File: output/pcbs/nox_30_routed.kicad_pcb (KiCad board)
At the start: 2 copper layers, 120.3 x 88.1 mm, 70 parts

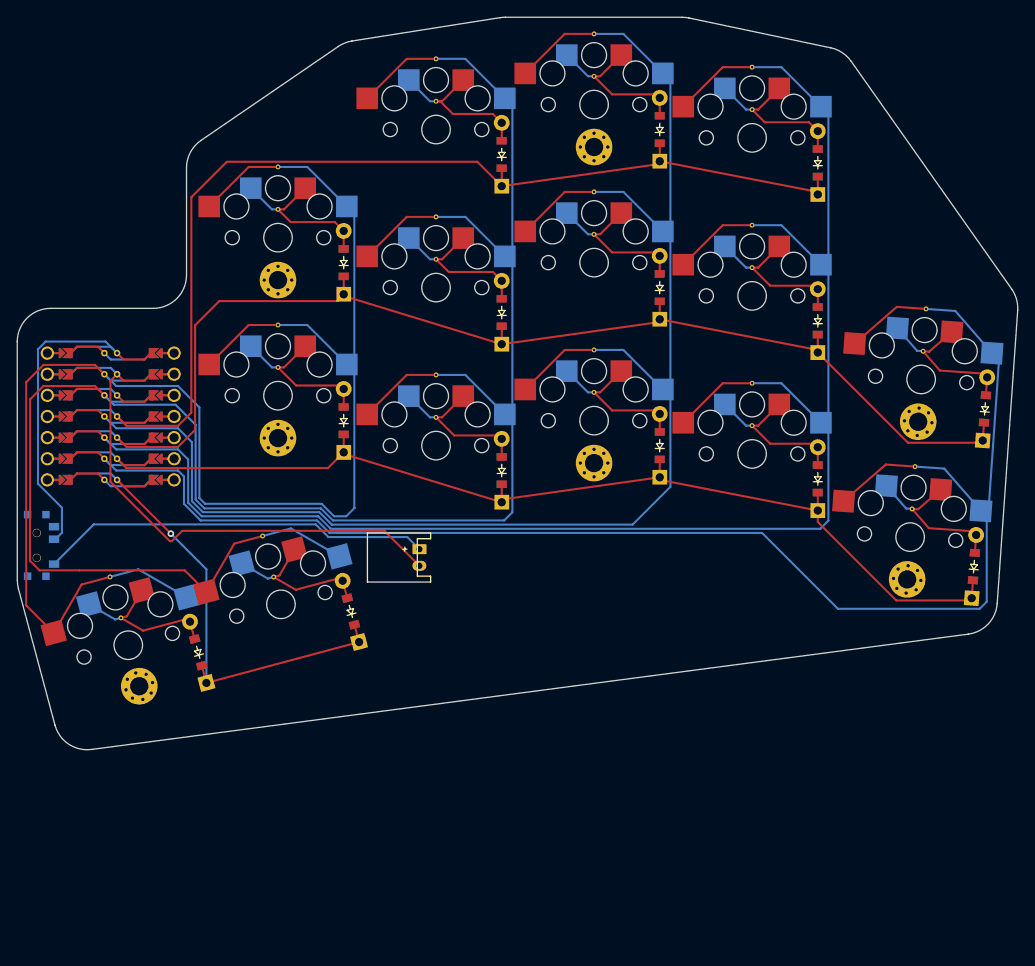
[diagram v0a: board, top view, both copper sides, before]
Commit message: 18 key layout
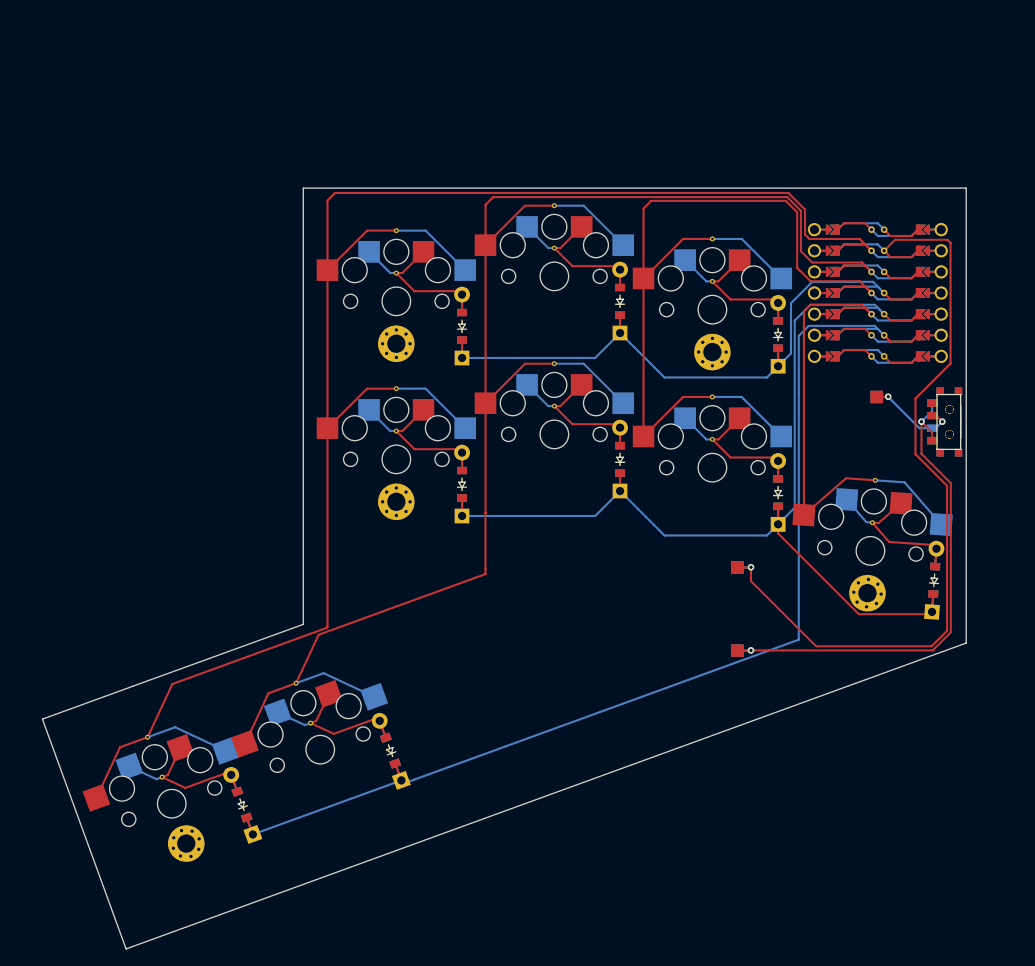
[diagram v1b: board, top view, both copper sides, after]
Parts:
- removed D10, D11, D12, D13, D14, D15: , ComboDiode
- removed JST1: , JST_PH_S2B-PH-K_02x2.00mm_Angled
- removed the REF** at (33.1, 90.2)
- removed the REF** at (50.1, 80.4)
- removed the REF** at (90.0, 58.0)
- removed the REF** at (71.0, 28.1)
- removed the REF** at (71.0, 42.0)
- removed the REF** at (128.5, 72.0)
- removed the REF** at (71.0, 23.0)
- removed the REF** at (52.0, 55.0)
- removed the REF** at (51.4, 85.3)
- removed the REF** at (71.0, 61.0)
- removed the REF** at (128.2, 77.1)
- removed the REF** at (109.0, 62.0)
- removed the REF** at (109.0, 67.1)
- removed the REF** at (109.0, 24.0)
- removed the REF** at (52.0, 60.1)
- removed the REF** at (90.0, 20.0)
- removed the REF** at (129.5, 58.2)
- removed the REF** at (90.0, 25.1)
- removed the REF** at (109.0, 48.1)
- removed the REF** at (109.0, 43.0)
- removed the REF** at (90.0, 44.1)
- removed the REF** at (90.0, 63.1)
- removed the REF** at (71.0, 66.1)
- removed the REF** at (90.0, 39.0)
- removed the REF** at (31.8, 85.3)
- removed the REF** at (52.0, 41.1)
- removed the REF** at (129.9, 53.1)
- removed the REF** at (52.0, 36.0)
- removed the REF** at (71.0, 47.1)
- removed the REF** at (109.0, 29.1)
- removed S10, S11, S12, S13, S14, S15: , PG1350
- removed _31, _32, _33, _34, _35, _36, _37: , MountingHole_2.2mm_M2_Pad_Via
- added BATTPAD1: , ComboDiode, F.Cu at (107.2, 89.2)
- added PAD1: , SMDPad, F.Cu at (123.9, 63.7)
- added REF**: VIA-0.6mm, VIA-0.6mm, F.Cu at (66.2, 62.7)
- added REF**: VIA-0.6mm, VIA-0.6mm, F.Cu at (85.2, 45.8)
- added REF**: VIA-0.6mm, VIA-0.6mm, F.Cu at (104.2, 44.7)
- added REF**: VIA-0.6mm, VIA-0.6mm, F.Cu at (85.2, 59.7)
- added REF**: VIA-0.6mm, VIA-0.6mm, F.Cu at (66.2, 43.7)
- added REF**: VIA-0.6mm, VIA-0.6mm, F.Cu at (123.4, 78.8)
- added REF**: VIA-0.6mm, VIA-0.6mm, F.Cu at (123.8, 73.7)
- added REF**: VIA-0.6mm, VIA-0.6mm, F.Cu at (104.2, 68.8)
- added REF**: VIA-0.6mm, VIA-0.6mm, F.Cu at (38.0, 109.4)
- added REF**: VIA-0.6mm, VIA-0.6mm, F.Cu at (66.2, 48.8)
- added REF**: VIA-0.6mm, VIA-0.6mm, F.Cu at (66.2, 67.8)
- added REF**: VIA-0.6mm, VIA-0.6mm, F.Cu at (36.3, 104.6)
- added REF**: VIA-0.6mm, VIA-0.6mm, F.Cu at (54.1, 98.1)
- added REF**: VIA-0.6mm, VIA-0.6mm, F.Cu at (85.2, 64.8)
- added REF**: VIA-0.6mm, VIA-0.6mm, F.Cu at (104.2, 63.7)
- added REF**: VIA-0.6mm, VIA-0.6mm, F.Cu at (85.2, 40.7)
- added REF**: VIA-0.6mm, VIA-0.6mm, F.Cu at (55.9, 102.9)
- added REF**: VIA-0.6mm, VIA-0.6mm, F.Cu at (104.2, 49.8)
- added T2: , E73:SPDT_C128955, F.Cu at (132.7, 66.7)
- added _19: , MountingHole_2.2mm_M2_Pad_Via, F.Cu at (66.2, 57.3)
- added _20: , MountingHole_2.2mm_M2_Pad_Via, F.Cu at (66.2, 76.3)
- added _21: , MountingHole_2.2mm_M2_Pad_Via, F.Cu at (104.2, 58.3)
- added _22: , MountingHole_2.2mm_M2_Pad_Via, F.Cu at (122.8, 87.3)
- added _23: , MountingHole_2.2mm_M2_Pad_Via, F.Cu at (40.9, 117.4)
- moved T1 110.7 mm to (132.7, 66.7), turned to -90 degrees
- moved S8 98.2 mm to (39.2, 112.6), turned to 20 degrees
- moved D8 95.5 mm to (47.6, 112.7), turned to 110 degrees
- moved xiao-ble1 93.4 mm to (115.2, 61.7)
- moved S9 62.9 mm to (57.0, 106.1), turned to 20 degrees
- moved D9 60.9 mm to (65.5, 106.2), turned to 110 degrees
- moved D5 52.5 mm to (112.1, 75.2)
- moved S5 52.5 mm to (104.2, 72.2)
- moved D7 48.2 mm to (130.9, 85.7), turned to 86 degrees
- moved S7 48.0 mm to (123.2, 82.2), turned to -4 degrees
- moved D6 19.5 mm to (112.1, 56.2)
- moved S6 19.5 mm to (104.2, 53.2)
- moved D2 16.2 mm to (74.1, 55.2)
- moved S2 16.2 mm to (66.2, 52.2)
- moved S1 16.2 mm to (66.2, 71.2)
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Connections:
- D1 pad 1: P8 -> P9
- D1 pad 2: inner_bottom -> index_home
- D2 pad 1: P9 -> P10
- D2 pad 2: inner_home -> index_top
- D3 pad 1: P8 -> P9
- D3 pad 2: index_bottom -> middle_home
- D4 pad 1: P9 -> P10
- D4 pad 2: index_home -> middle_top
- D5 pad 1: P10 -> P9
- D5 pad 2: index_top -> ring_home
- D6 pad 1: P8 -> P10
- D6 pad 2: middle_bottom -> ring_top
- D7 pad 2: middle_home -> pinky_home
- D8 pad 1: P10 -> P8
- D8 pad 2: middle_top -> one_main
- D9 pad 2: ring_bottom -> two_main
- S1 pad 1: inner_bottom -> index_home
- S2 pad 1: inner_home -> index_top
- S3 pad 1: index_bottom -> middle_home
- S4 pad 1: index_home -> middle_top
- S5 pad 1: index_top -> ring_home
- S5 pad 2: P2 -> P3
- S6 pad 1: middle_bottom -> ring_top
- S7 pad 1: middle_home -> pinky_home
- S7 pad 2: P3 -> P4
- S8 pad 1: middle_top -> one_main
- S8 pad 2: P3 -> P1
- S9 pad 1: ring_bottom -> two_main
- S9 pad 2: P4 -> P2
- T1 pad 2: VCC5 -> RAW
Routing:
- net P5: track 187.8 -> 0.00 mm
- net P4: track 208.1 -> 53.9 mm
- net P3: track 192.5 -> 104.7 mm
- net P2: track 246.8 -> 187.0 mm
- net P7: track 52.2 -> 0.00 mm, vias 1 -> 0
- net P10: track 121.6 -> 76.0 mm
- net GND: track 55.6 -> 91.2 mm, vias 0 -> 1
- net VCC5: track 35.0 -> 0.00 mm
- net P1: track 185.0 -> 210.1 mm
- net index_bottom: track 19.8 -> 0.00 mm
- net inner_bottom: track 19.8 -> 0.00 mm
- net ring_bottom: track 19.8 -> 0.00 mm
- net middle_bottom: track 19.8 -> 0.00 mm
- net pinky_bottom: track 19.8 -> 0.00 mm
- net inner_home: track 19.8 -> 0.00 mm
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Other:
- board size 120.3 x 88.1 mm -> 111.1 x 91.5 mm
